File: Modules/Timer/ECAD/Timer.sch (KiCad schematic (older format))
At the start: 19 parts, among them J1 comm_header, J2 prog_header, U1 ATmega328-PU, U2 KCSC02-105, U3 KCSC02-105, U4 MAX7219, U5 KCSC02-105, U6 KCSC02-105

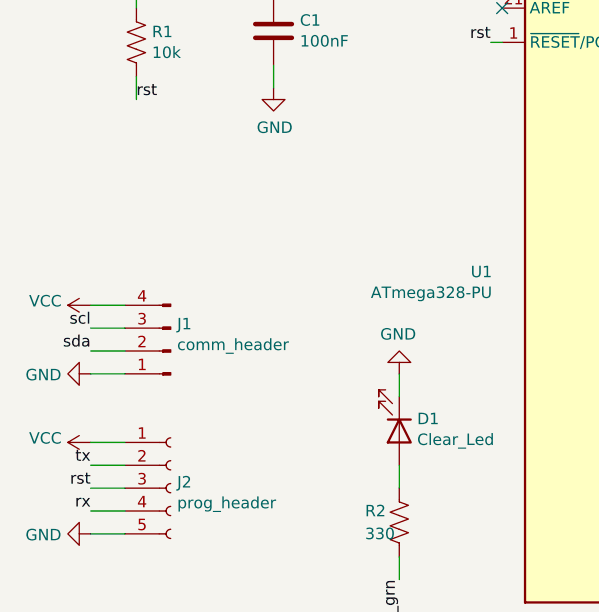
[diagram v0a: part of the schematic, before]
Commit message: Added polyfuses to all modules
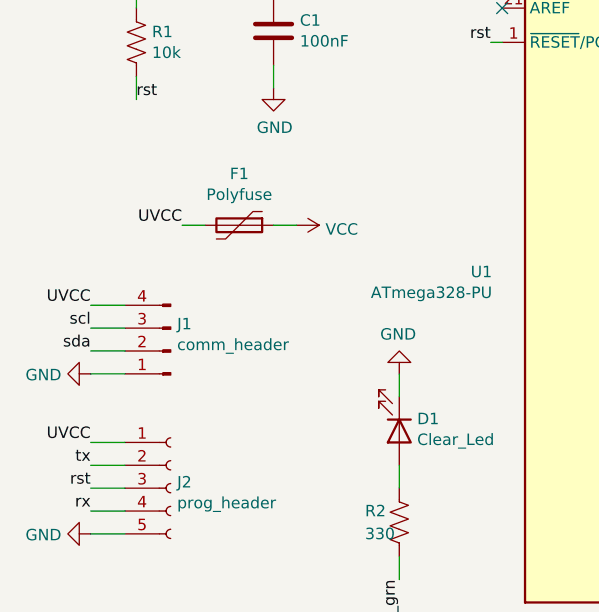
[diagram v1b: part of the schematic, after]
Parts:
- added F1: Polyfuse, symbol Device:Polyfuse
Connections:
- net VCC: now also F1.1; no longer J1.4 (Pin_4), J2.1 (Pin_1)
- new net UVCC: F1.2, J1.4 (Pin_4), J2.1 (Pin_1)
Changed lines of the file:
@@
 EESchema Schematic File Version 4
 LIBS:Timer-cache
-LIBS:MorseCode-cache
 EELAYER 29 0
 EELAYER END
@@
 L power:VCC #PWR01
 U 1 1 5F822FD5
-P 1400 3350
-F 0 "#PWR01" H 1400 3200 50  0001 C CNN
-F 1 "VCC" V 1418 3477 50  0000 L CNN
-F 2 "" H 1400 3350 50  0001 C CNN
-F 3 "" H 1400 3350 50  0001 C CNN
-	1    1400 3350
-	0    -1   -1   0
-$EndComp
-$Comp
-L power:VCC #PWR03
-U 1 1 5F822FD6
-P 1400 3950
-F 0 "#PWR03" H 1400 3800 50  0001 C CNN
-F 1 "VCC" V 1418 4077 50  0000 L CNN
-F 2 "" H 1400 3950 50  0001 C CNN
-F 3 "" H 1400 3950 50  0001 C CNN
-	1    1400 3950
-	0    -1   -1   0
+P 2300 3000
+F 0 "#PWR01" H 2300 2850 50  0001 C CNN
+F 1 "VCC" V 2318 3127 50  0000 L CNN
+F 2 "" H 2300 3000 50  0001 C CNN
+F 3 "" H 2300 3000 50  0001 C CNN
+	1    2300 3000
+	0    1    1    0
 $EndComp
 $Comp
@@
 	6100 4700 6100 5050
 NoConn ~ 4400 3950
+$Comp
+L Device:Polyfuse F1
+U 1 1 5F922CA4
+P 2050 3000
+F 0 "F1" V 1825 3000 50  0000 C CNN
+F 1 "Polyfuse" V 1916 3000 50  0000 C CNN
+F 2 "" H 2100 2800 50  0001 L CNN
+F 3 "~" H 2050 3000 50  0001 C CNN
+	1    2050 3000
+	0    1    1    0
+$EndComp
+Text Label 1400 3350 2    50   ~ 0
+UVCC
+Text Label 1400 3950 2    50   ~ 0
+UVCC
+Text Label 1800 3000 2    50   ~ 0
+UVCC
+Wire Wire Line
+	1800 3000 1900 3000
+Wire Wire Line
+	2200 3000 2300 3000
 $EndSCHEMATC

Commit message: Updated timer schematic
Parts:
- removed D4: Strike_1, symbol Device:LED
- removed D5: Strike_2, symbol Device:LED
- added CSet1: 22p, symbol Device:C
- added R?: 330, symbol Device:R_US
- added RSet2: 56k, symbol Device:R_US
- added U7: DFPLAYER_MINI, symbol rur:DFPLAYER_MINI
- added U8: MAX6954, Package_DIP:DIP-40_W15.24mm, symbol Driver_LED:MAX6954
- added U9: XAMR14C2, symbol Display_Character:XAMR14C2
- added U?: NodeMCU_ESP-32S, Module:NodeMCU_ESP-32S, symbol MCU_Module:NodeMCU_ESP-32S
- U1: symbol MCU_Microchip_ATmega:ATmega328-PU -> Timer-rescue:ATmega328-PU-MCU_Microchip_ATmega
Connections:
- net GND: now also CSet1.1, RSet2.2, U7.7 (GND), U8.17 (GND), U8.18 (GND), U8.20 (GND), U?.14 (GND), U?.32 (GND), U?.38 (GND); no longer LS1.1
- net VCC: now also U7.1 (VCC), U8.21 (V+), U8.23 (V+), U8.24 (V+)
- net at U1.12 (PD6): no longer LS1.2
- net at U1.14 (PB0), U4.1 (DIN): now also U8.6 (DIN)
- net at U1.15 (PB1), U4.13 (CLK): now also U8.5 (CLK)
- net at U1.17 (MOSI/PB3): now also U8.3 (~CS)
- net at U1.18 (MISO/PB4): now also U7.2 (RX)
- net at U1.19 (SCK/PB5): now also U7.3 (TX)
- net at U1.4 (PD2): now also R?.2
- net at D2.2 (A), D3.2 (A): no longer U1.5 (PD3)
- net at U1.6 (PD4): now also U?.28 (TX2/IO17)
- new net: U1.5 (PD3), U?.27 (RX2/IO16)
- new net: LS1.1, U7.6 (SPK_1)
- new net: LS1.2, U7.8 (SPK_2)
- new net: U8.11 (O4), U9.10 (B)
- new net: U8.12 (O5), U9.9 (C)
- new net: U8.13 (O6), U9.7 (D)
- new net: U8.15 (O8), U9.1 (E)
- new net: RSet2.1, U8.19 (ISET)
- new net: CSet1.2, U8.22 (OSC)
- new net: U8.26 (O9), U9.18 (F)
- new net: U8.29 (O12), U9.17 (G)
- new net: U8.30 (O13), U9.15 (H)
- new net: U8.31 (O14), U9.14 (J)
- new net: U8.32 (O15), U9.5 (L)
- new net: U8.33 (O16), U9.4 (M)
- new net: U8.34 (O17), U9.2 (N)
- new net: U8.35 (O18), U9.8 (DP)
- new net: U8.9 (O2), U9.12 (A)
- new net O0: U8.7 (O0), U9.16 (DIG_1)
- new net O1: U8.8 (O1), U9.11 (DIG_2)
- new net O10: U8.27 (O10), U9.13 (P)
- new net O11: U8.28 (O11), U9.6 (K)
- no-connect marks 20 -> 71
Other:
- moved on the sheet: C2, D2, D3, LS1, RSet1, U2, U3, U4, U5, U6

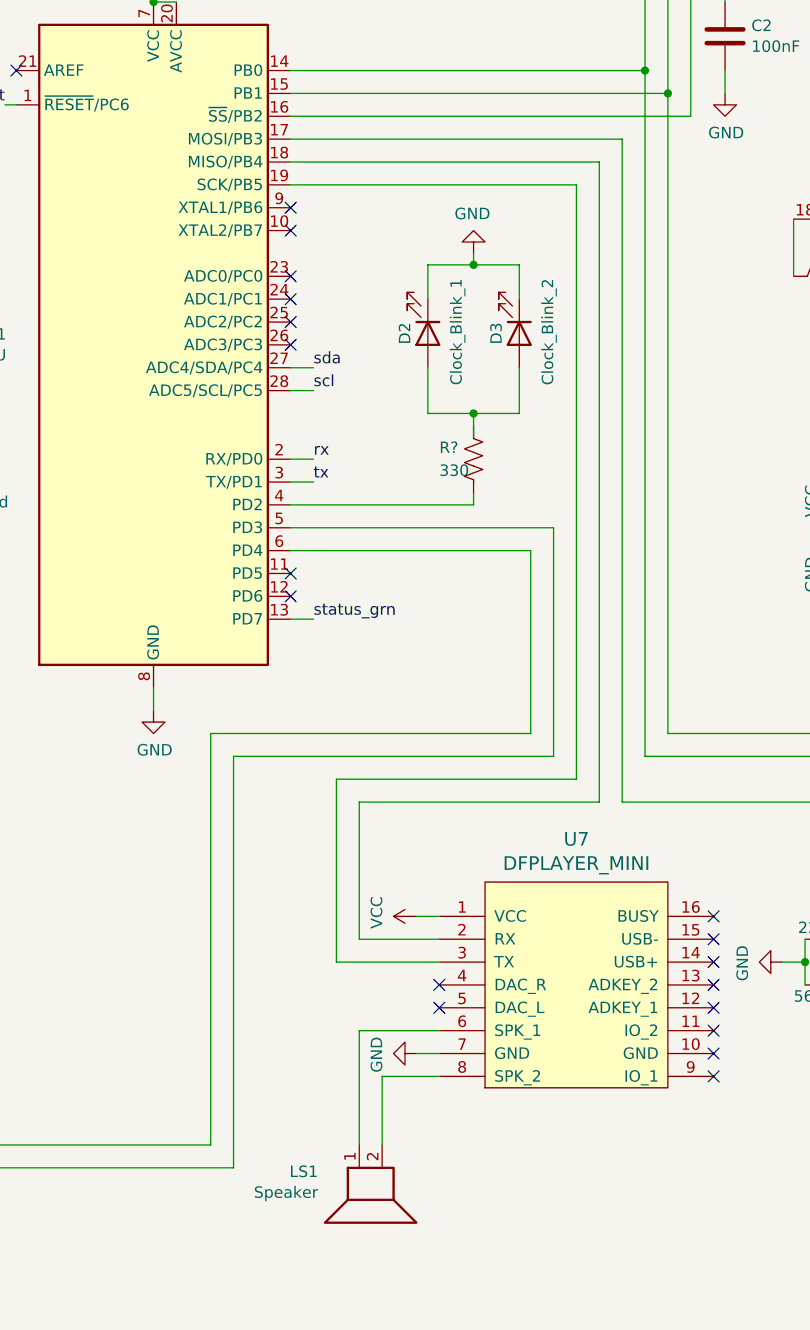
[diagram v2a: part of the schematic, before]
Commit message: Added voltage divider to safely communicate with DFPlayer
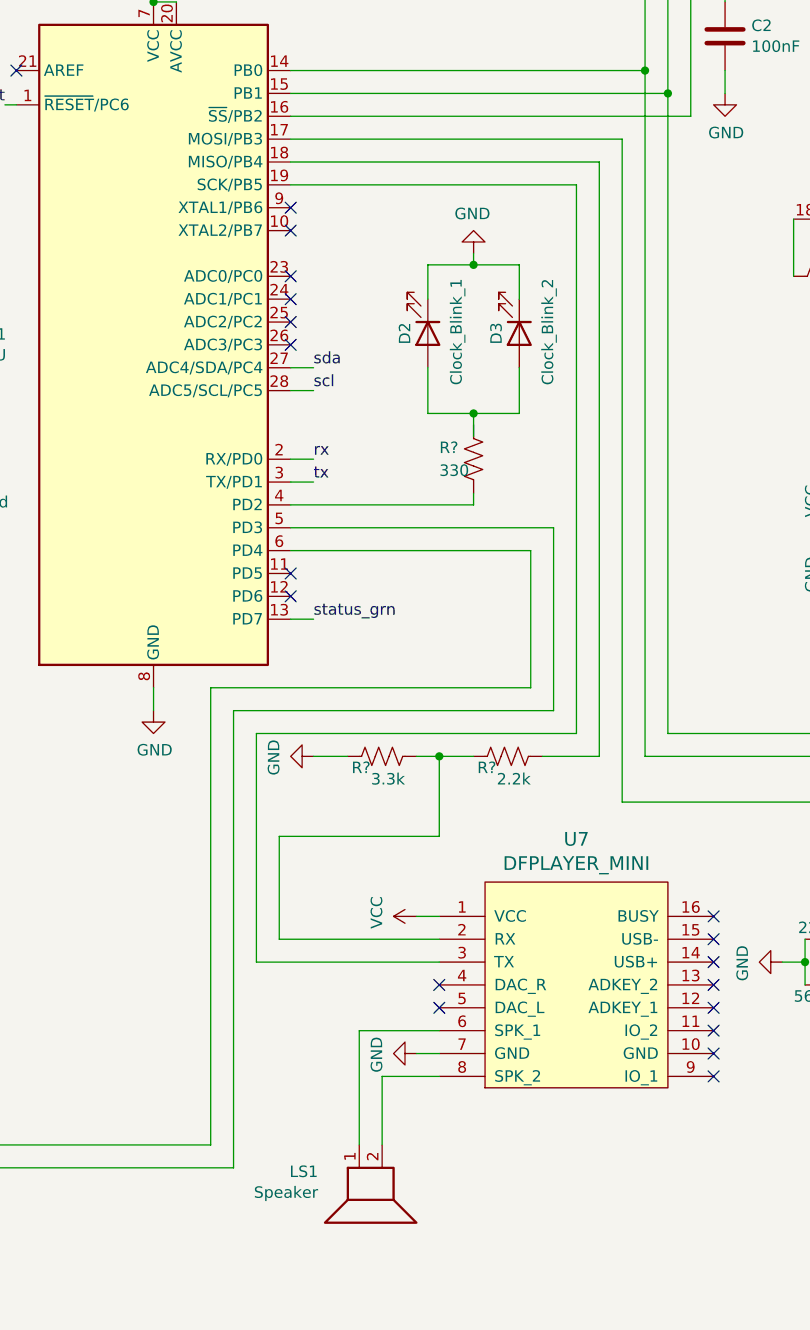
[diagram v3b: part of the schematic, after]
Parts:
- added R?: 2.2k, symbol Device:R_US
- added R?: 3.3k, symbol Device:R_US
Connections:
- net GND: now also R?.1
- net at U1.18 (MISO/PB4): now also R?.2; no longer U7.2 (RX)
- new net: R?.1, R?.2, U7.2 (RX)
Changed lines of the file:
@@
 	4700 6250 5050 6250
 Wire Wire Line
-	5050 5850 4700 5850
+	5050 5850 4350 5850
 Wire Wire Line
-	4700 5850 4700 5250
-Wire Wire Line
-	5750 5250 5750 2450
+	5750 5050 5750 2450
 Wire Wire Line
 	5750 2450 4400 2450
 Wire Wire Line
-	4700 5250 5750 5250
-Wire Wire Line
 	4400 2550 5650 2550
 Wire Wire Line
-	5650 2550 5650 5150
+	5650 2550 5650 4950
 Wire Wire Line
-	5650 5150 4600 5150
+	5650 4950 4250 4950
 Wire Wire Line
-	4600 5150 4600 5950
+	4250 4950 4250 5950
 Wire Wire Line
-	4600 5950 5050 5950
+	4250 5950 5050 5950
 NoConn ~ 4400 4250
 NoConn ~ 4400 4350
@@
 	4400 4050 5550 4050
 Wire Wire Line
-	5550 4050 5550 5050
+	5550 4050 5550 4850
 Wire Wire Line
-	5550 5050 4150 5050
+	5550 4850 4150 4850
 Wire Wire Line
-	4150 5050 4150 6850
+	4150 4850 4150 6850
 Wire Wire Line
 	4150 6850 2900 6850
@@
 	2900 6750 4050 6750
 Wire Wire Line
-	4050 6750 4050 4950
+	4050 6750 4050 4750
 Wire Wire Line
-	4050 4950 5450 4950
+	4050 4750 5450 4750
 Wire Wire Line
-	5450 4950 5450 4150
+	5450 4750 5450 4150
 Wire Wire Line
 	5450 4150 4400 4150
@@
 	1800 7550 1800 7450
 NoConn ~ 700  5150
+$Comp
+L Device:R_US R?
+U 1 1 60BAF373
+P 5350 5050
+F 0 "R?" V 5300 5100 50  0000 L CNN
+F 1 "2.2k" V 5250 4950 50  0000 L CNN
+F 2 "" V 5390 5040 50  0001 C CNN
+F 3 "~" H 5350 5050 50  0001 C CNN
+	1    5350 5050
+	0    -1   -1   0
+$EndComp
+$Comp
+L Device:R_US R?
+U 1 1 60BF9C18
+P 4800 5050
+F 0 "R?" V 4750 5100 50  0000 L CNN
+F 1 "3.3k" V 4700 4950 50  0000 L CNN
+F 2 "" V 4840 5040 50  0001 C CNN
+F 3 "~" H 4800 5050 50  0001 C CNN
+	1    4800 5050
+	0    -1   -1   0
+$EndComp
+$Comp
+L power:GND #PWR?
+U 1 1 60BFA871
+P 4500 5050
+AR Path="/5F832F87/60BFA871" Ref="#PWR?"  Part="1"
+AR Path="/60BFA871" Ref="#PWR?"  Part="1"
+F 0 "#PWR?" H 4500 4800 50  0001 C CNN
+F 1 "GND" H 4505 4877 50  0000 C CNN
+F 2 "" H 4500 5050 50  0001 C CNN
+F 3 "" H 4500 5050 50  0001 C CNN
+	1    4500 5050
+	0    1    1    0
+$EndComp
+Wire Wire Line
+	4650 5050 4500 5050
+Wire Wire Line
+	5500 5050 5750 5050
+Wire Wire Line
+	5200 5050 5050 5050
+Wire Wire Line
+	5050 5050 5050 5400
+Wire Wire Line
+	5050 5400 4350 5400
+Wire Wire Line
+	4350 5400 4350 5850
+Connection ~ 5050 5050
+Wire Wire Line
+	5050 5050 4950 5050
 $EndSCHEMATC

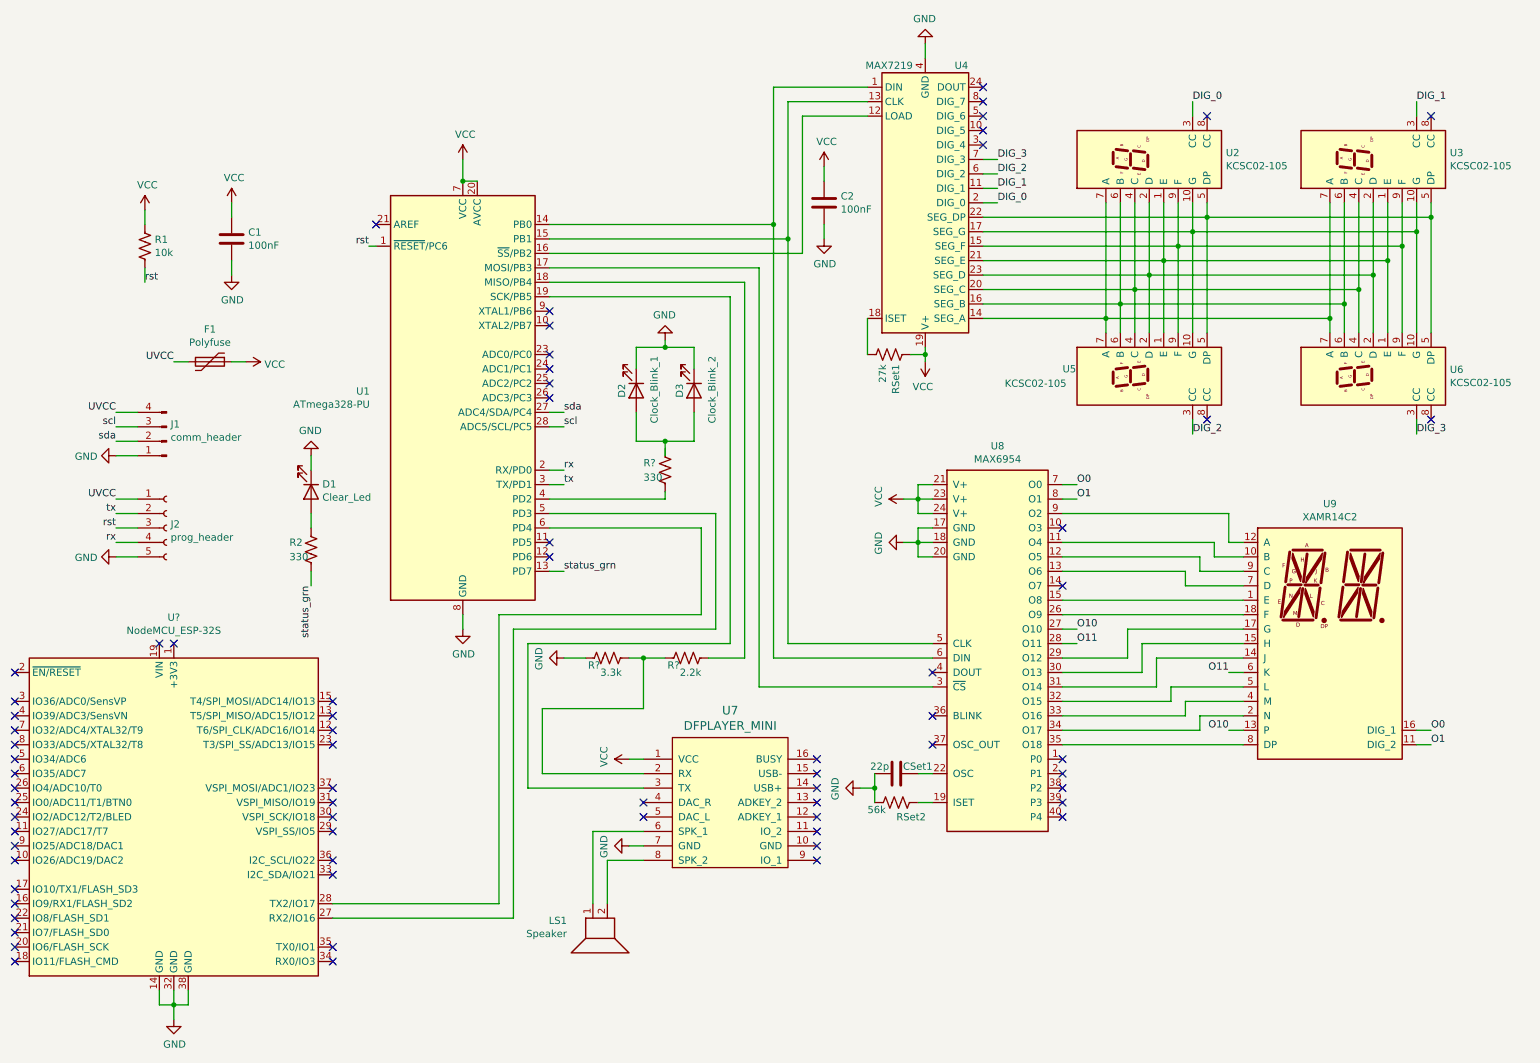
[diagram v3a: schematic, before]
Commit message: Added pullup resistors to I2C lines
Also add resistor for clock dot
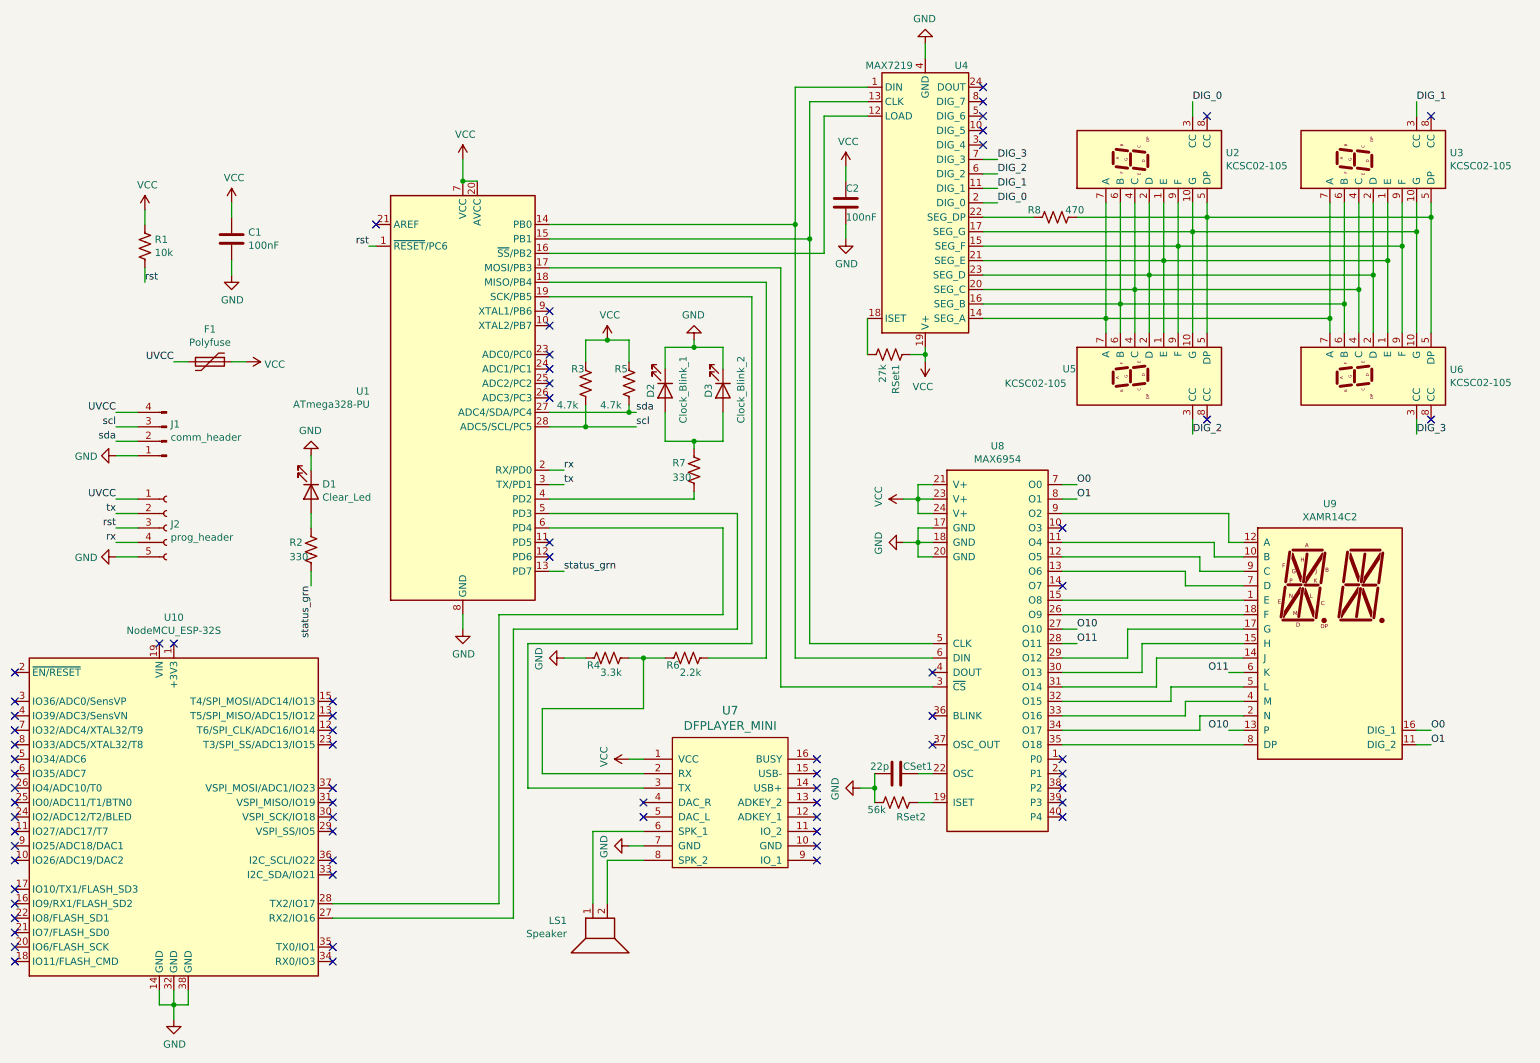
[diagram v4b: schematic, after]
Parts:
- added R3, R5: 4.7k, symbol Device:R_US
- added R8: 470, symbol Device:R_US
- gave numbers to parts that had none: 4
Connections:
- net VCC: now also R3.1, R5.1
- net scl: now also R3.2
- net sda: now also R5.2
- net at U2.5 (DP), U3.5 (DP), U5.5 (DP)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: now also R8.2; no longer U4.22 (SEG_DP)
- net at D2.2 (A), D3.2 (A): now also R7.1
- new net: R8.1, U4.22 (SEG_DP)
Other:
- moved on the sheet: C2, D2, D3, R7
